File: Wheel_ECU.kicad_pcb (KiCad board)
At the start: 2 copper layers, 61 x 61 mm, 57 parts, among them J1 Conn_01x04, J2 Conn_01x04, J3 Conn_01x02, J4 Debug, U1 IFX9201SG, U2 TLE4964, U3 XMC1404_F064, U4 TLE7251

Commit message: Increase motor hole again and remove two mount holes
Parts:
- removed the M** at (140.1, 90.1)
- removed the M** at (123.5, 106.7)
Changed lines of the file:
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@@
     (tracks 440)
     (zones 0)
-    (modules 57)
+    (modules 55)
     (nets 63)
   )
@@
     (mod_text_size 1 1)
     (mod_text_width 0.15)
-    (pad_size 11.55 5)
-    (pad_drill 9.75)
+    (pad_size 10 10)
+    (pad_drill 10)
     (pad_to_mask_clearance 0.2)
     (aux_axis_origin 0 0)
@@
       (effects (font (size 1 1) (thickness 0.15)))
     )
-    (pad "" np_thru_hole circle (at 0 0) (size 10 10) (drill 10) (layers *.Cu *.Mask)
-      (solder_mask_margin 0.5) (clearance 0.75))
+    (pad "" np_thru_hole circle (at 0 0) (size 10 10) (drill 10) (layers *.Cu *.Mask))
+  )
+  (module WheelECU:Mount_Hole_M3x6.5 (layer F.Cu)
+    (at 123.5 90.1 135)
+    (fp_text reference M** (at -1.2 3.2 135) (layer F.SilkS) hide
+      (effects (font (size 1 1) (thickness 0.15)))
+    )
+    (fp_text value Motor_Mount_Hole (at 0 -3.5 135) (layer F.Fab) hide
+      (effects (font (size 1 1) (thickness 0.15)))
+    )
+    (pad "" np_thru_hole oval (at 0 0 135) (size 9.75 3.2) (drill oval 9.75 3.2) (layers *.Cu *.Mask)
+      (solder_mask_margin 1.2) (clearance 1.4))
   )
   (module Diodes_SMD:D_MELF (layer F.Cu)
@@
   )
   (module WheelECU:Mount_Hole_M3x6.5 (layer F.Cu)
-    (at 140.1 90.1 45)
-    (fp_text reference M** (at -1.2 3.2 45) (layer F.SilkS) hide
-      (effects (font (size 1 1) (thickness 0.15)))
-    )
-    (fp_text value Motor_Mount_Hole (at 0 -3.5 45) (layer F.Fab) hide
-      (effects (font (size 1 1) (thickness 0.15)))
-    )
-    (pad "" np_thru_hole oval (at 0 0 45) (size 9.75 3.2) (drill oval 9.75 3.2) (layers *.Cu *.Mask)
-      (solder_mask_margin 1.2) (clearance 1.4))
-  )
-  (module WheelECU:Mount_Hole_M3x6.5 (layer F.Cu)
-    (at 123.5 106.7 45)
-    (fp_text reference M** (at -1.2 3.2 45) (layer F.SilkS) hide
-      (effects (font (size 1 1) (thickness 0.15)))
-    )
-    (fp_text value Motor_Mount_Hole (at 0 -3.5 45) (layer F.Fab) hide
-      (effects (font (size 1 1) (thickness 0.15)))
-    )
-    (pad "" np_thru_hole oval (at 0 0 45) (size 9.75 3.2) (drill oval 9.75 3.2) (layers *.Cu *.Mask)
-      (solder_mask_margin 1.2) (clearance 1.4))
-  )
-  (module WheelECU:Mount_Hole_M3x6.5 (layer F.Cu)
-    (at 123.5 90.1 135)
-    (fp_text reference M** (at -1.2 3.2 135) (layer F.SilkS) hide
-      (effects (font (size 1 1) (thickness 0.15)))
-    )
-    (fp_text value Motor_Mount_Hole (at 0 -3.5 135) (layer F.Fab) hide
-      (effects (font (size 1 1) (thickness 0.15)))
-    )
-    (pad "" np_thru_hole oval (at 0 0 135) (size 9.75 3.2) (drill oval 9.75 3.2) (layers *.Cu *.Mask)
-      (solder_mask_margin 1.2) (clearance 1.4))
-  )
-  (module WheelECU:Mount_Hole_M3x6.5 (layer F.Cu)

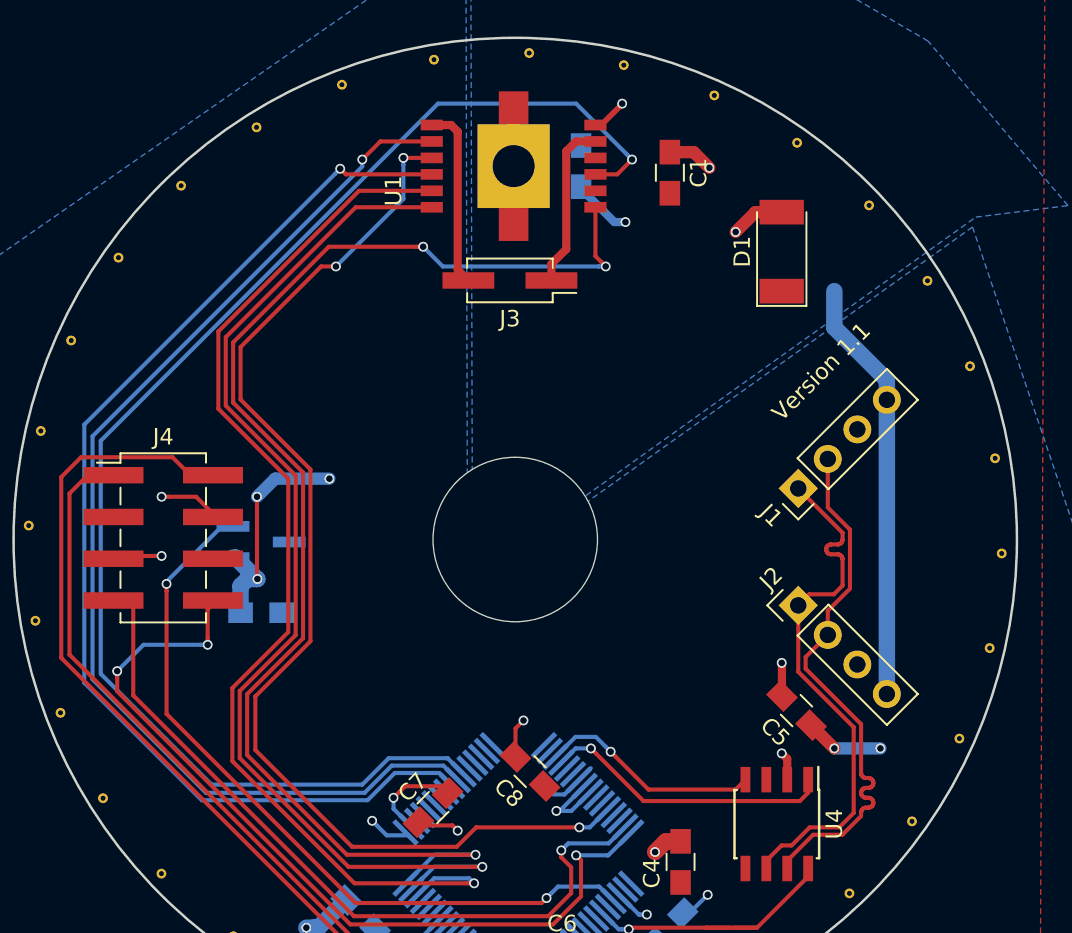
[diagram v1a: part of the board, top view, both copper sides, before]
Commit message: Supply the motor directly from the battery
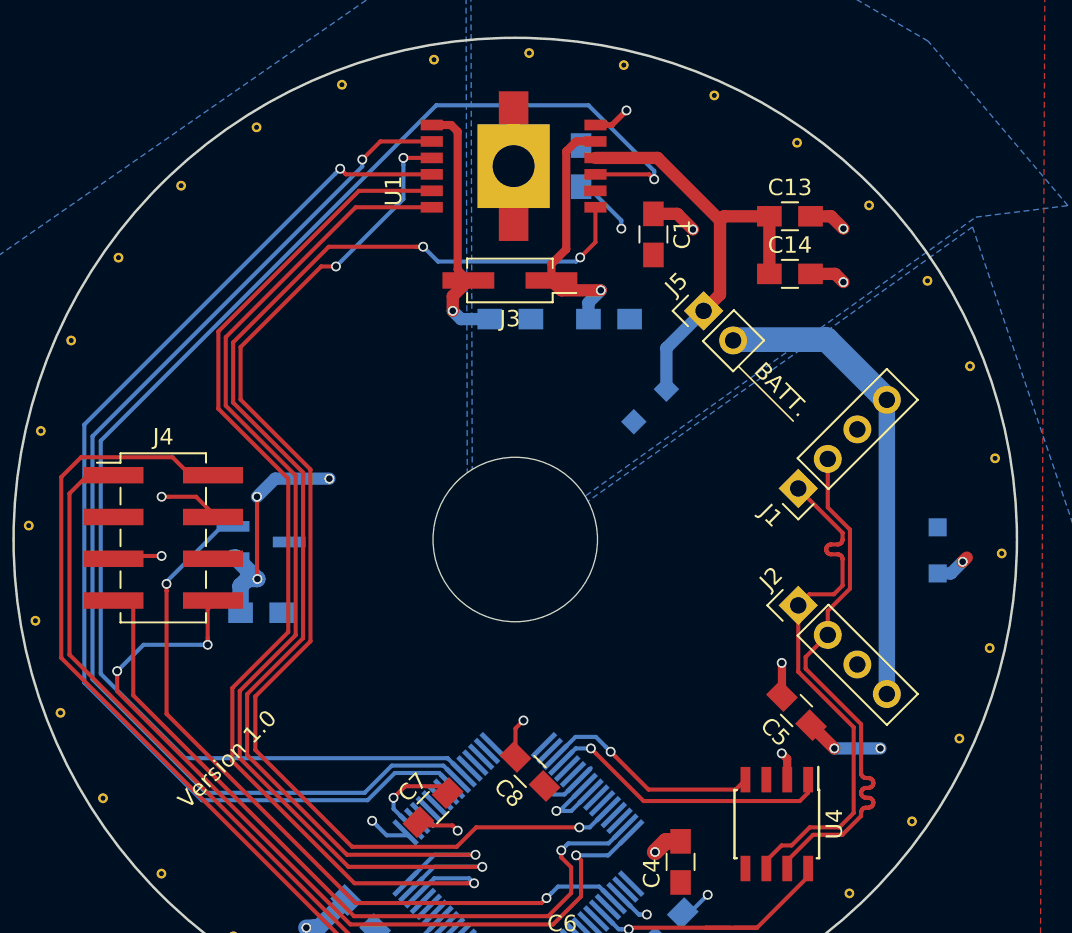
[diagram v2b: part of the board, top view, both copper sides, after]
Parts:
- added C11: 30nF, WheelECU:C_0805_HandSoldering, B.Cu at (131.5, 85.0)
- added C12: 30nF, WheelECU:C_0805_HandSoldering, B.Cu at (137.5, 85.0)
- added C13: 100uF, WheelECU:C_0805_HandSoldering, F.Cu at (148.5, 78.8)
- added C14: 100nF, WheelECU:C_0805_HandSoldering, F.Cu at (148.5, 82.2)
- added D2: SMF36A, Diode_SMD:D_SOD-123F, B.Cu at (140.0, 90.2)
- added J5: Conn_01x02, Connector_PinHeader_2.54mm:PinHeader_1x02_P2.54mm_Vertical, F.Cu at (143.2, 84.5)
- D1: footprint Diodes_SMD:D_MELF -> Diode_SMD:D_SOD-123F; moved to B.Cu
- moved D1 20.5 mm to (157.5, 99.1)
- moved C1 3.88 mm to (140.2, 79.8)
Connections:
- U1 pad 4: +5V -> +BATT
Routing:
- net +BATT: track 0.00 -> 27.4 mm
- net MOTOR_OUT1: track 10.2 -> 15.6 mm, vias 0 -> 1
- net MOTOR_OUT2: track 11.1 -> 15.8 mm, vias 0 -> 1
- net GND: track 77.9 -> 82.2 mm, vias 12 -> 13
- net +5V: track 44.8 -> 47.1 mm, vias 12 -> 13
- net MOTOR_DIRECTION: track 78.8 -> 76.8 mm
- net MISO: track 85.0 -> 86.8 mm
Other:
- board text added: "BATT."
- board text added: "Version 1.0"
- board text removed: "Version 1.1"

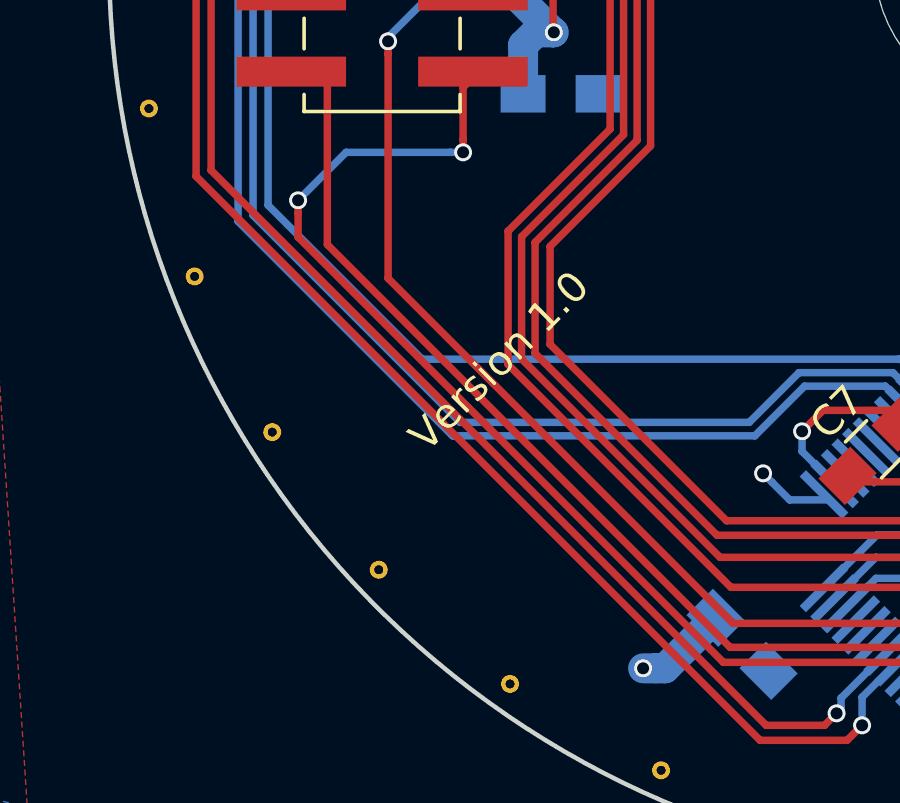
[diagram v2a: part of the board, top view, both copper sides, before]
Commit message: Update the name and version text on the PCB
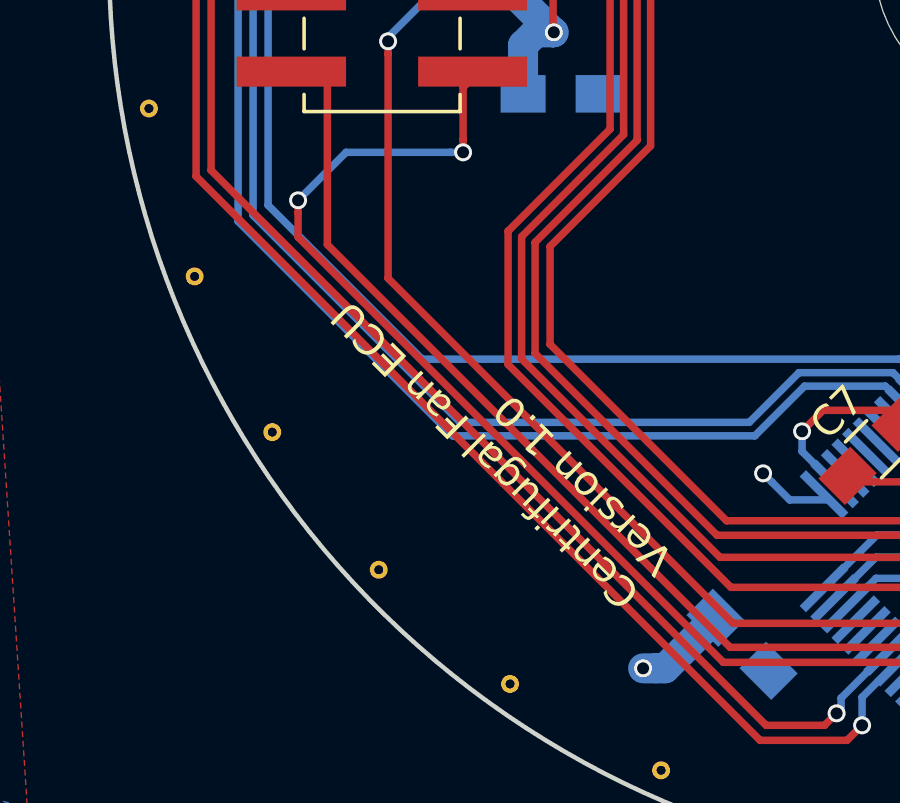
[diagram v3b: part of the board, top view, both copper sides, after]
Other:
- board text added: "Centrifugal Fan ECU Version 1.0"
- board text removed: "Version 1.0"
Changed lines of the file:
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@@
     (arrow2b (pts (xy 101.3 59.5) (xy 102.426504 58.913579)))
   )
-  (gr_text "Version 1.0" (at 114.3 111.76 45) (layer F.SilkS)
-    (effects (font (size 1 1) (thickness 0.15)))
+  (gr_text "Centrifugal Fan ECU\nVersion 1.0" (at 119.3 119.2 135) (layer F.SilkS)
+    (effects (font (size 1 1) (thickness 0.15)) (justify left))
   )
   (segment (start 154.392103 107.792103) (end 154.392103 89.907897) (width 1) (layer B.Cu) (net 1))

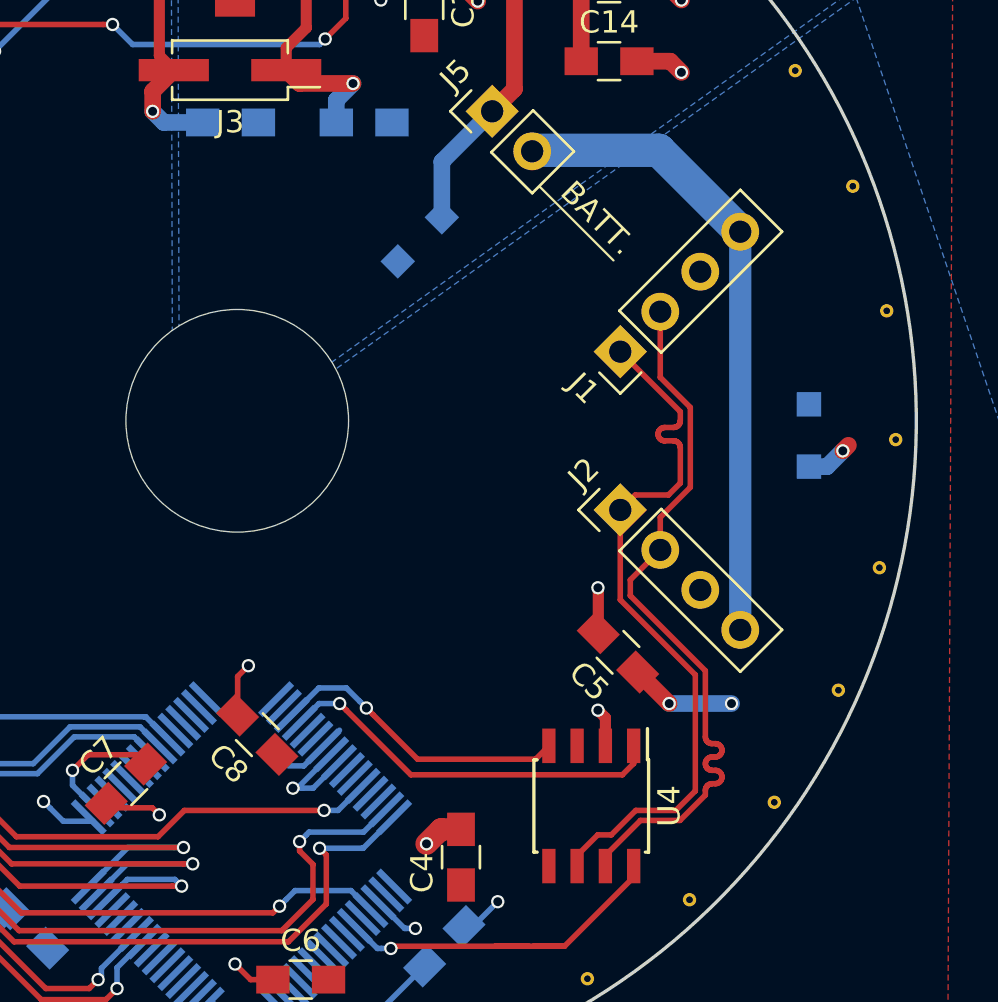
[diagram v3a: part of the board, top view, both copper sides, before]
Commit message: Make room for a bigger motor on the PCB
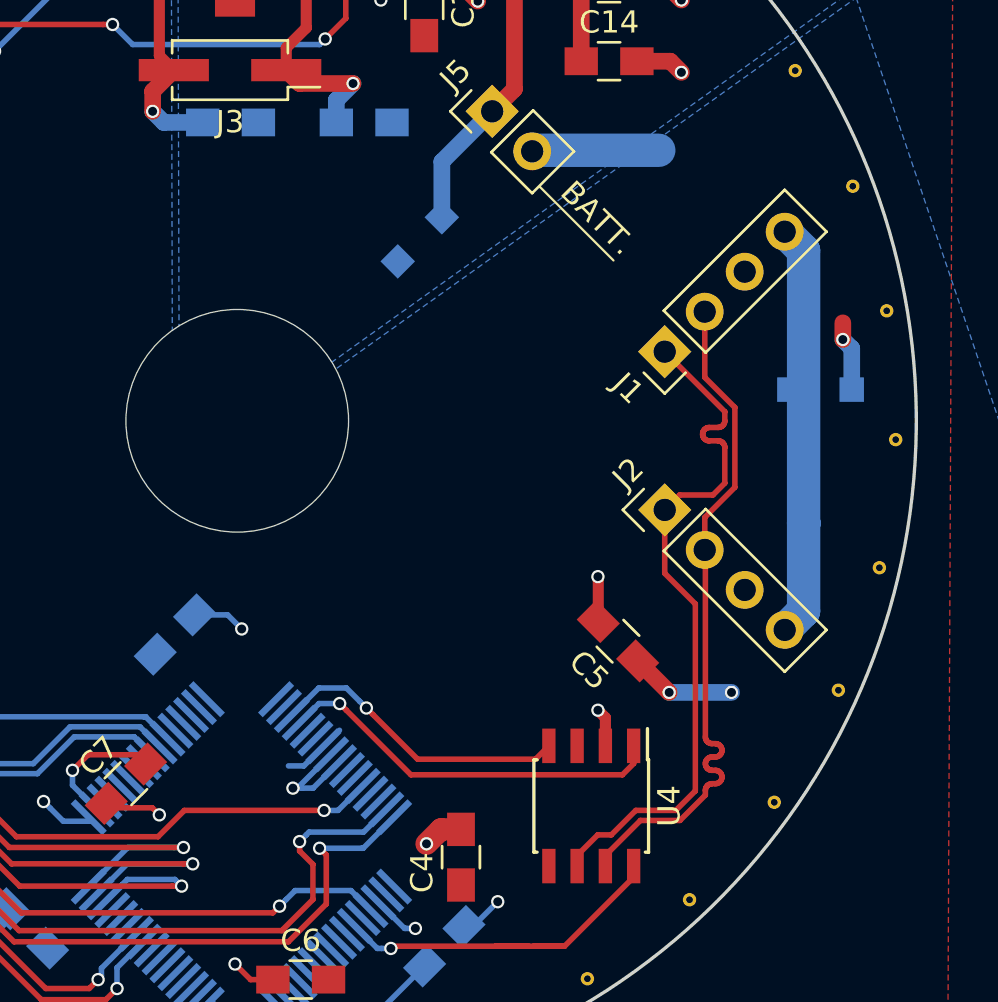
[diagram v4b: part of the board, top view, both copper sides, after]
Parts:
- C8: moved to B.Cu
- moved C8 5.83 mm to (129.0, 108.0), turned to 45 degrees
- moved D1 2.12 mm to (158.0, 97.0), turned to 180 degrees
- moved J1 2.00 mm to (151.0, 95.3)
- moved J2 2.00 mm to (151.0, 102.4)
- moved C5 0.50 mm to (148.9, 108.3)
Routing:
- net GND: track 82.2 -> 75.3 mm, vias 13 -> 12
- net +5V: track 47.1 -> 50.5 mm, vias 13 -> 14
- net CAN+: track 32.8 -> 30.9 mm
- net CAN-: track 32.7 -> 31.9 mm

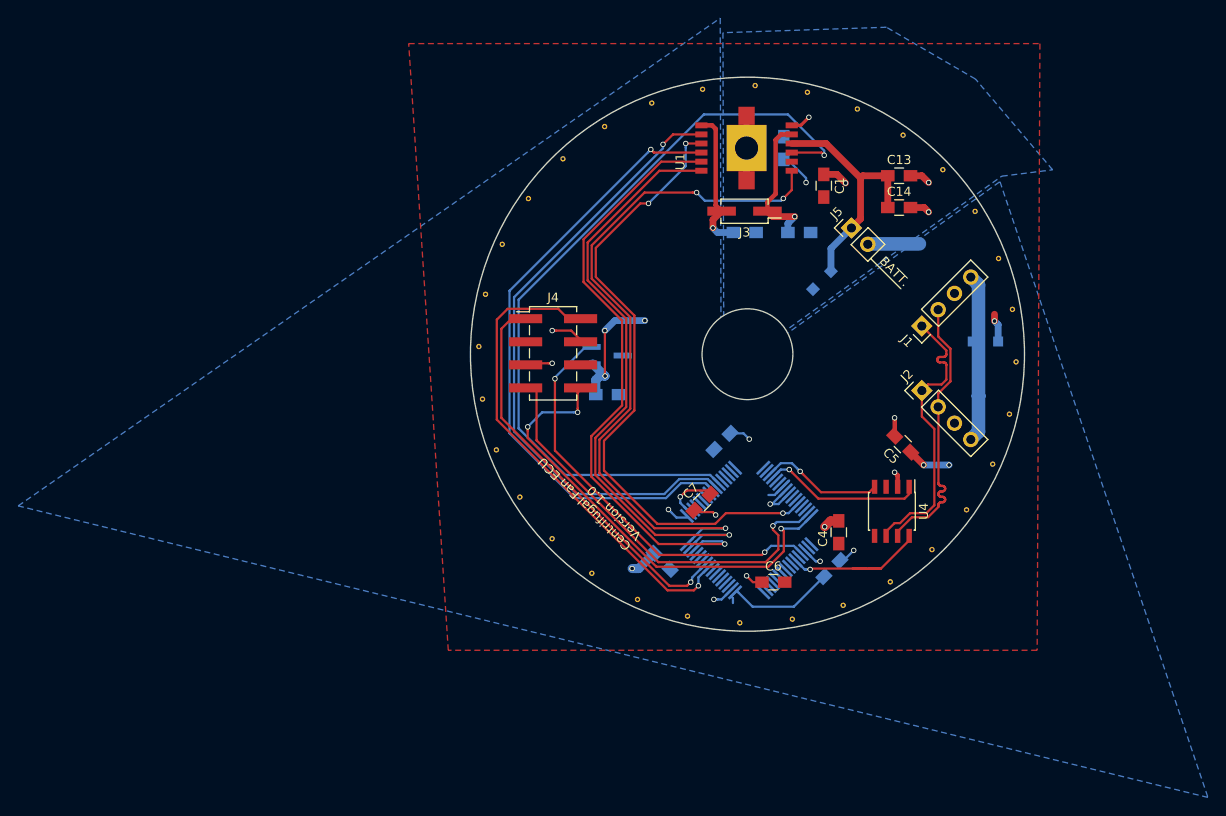
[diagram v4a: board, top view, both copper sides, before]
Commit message: Improve the placement of the motor driver and connector
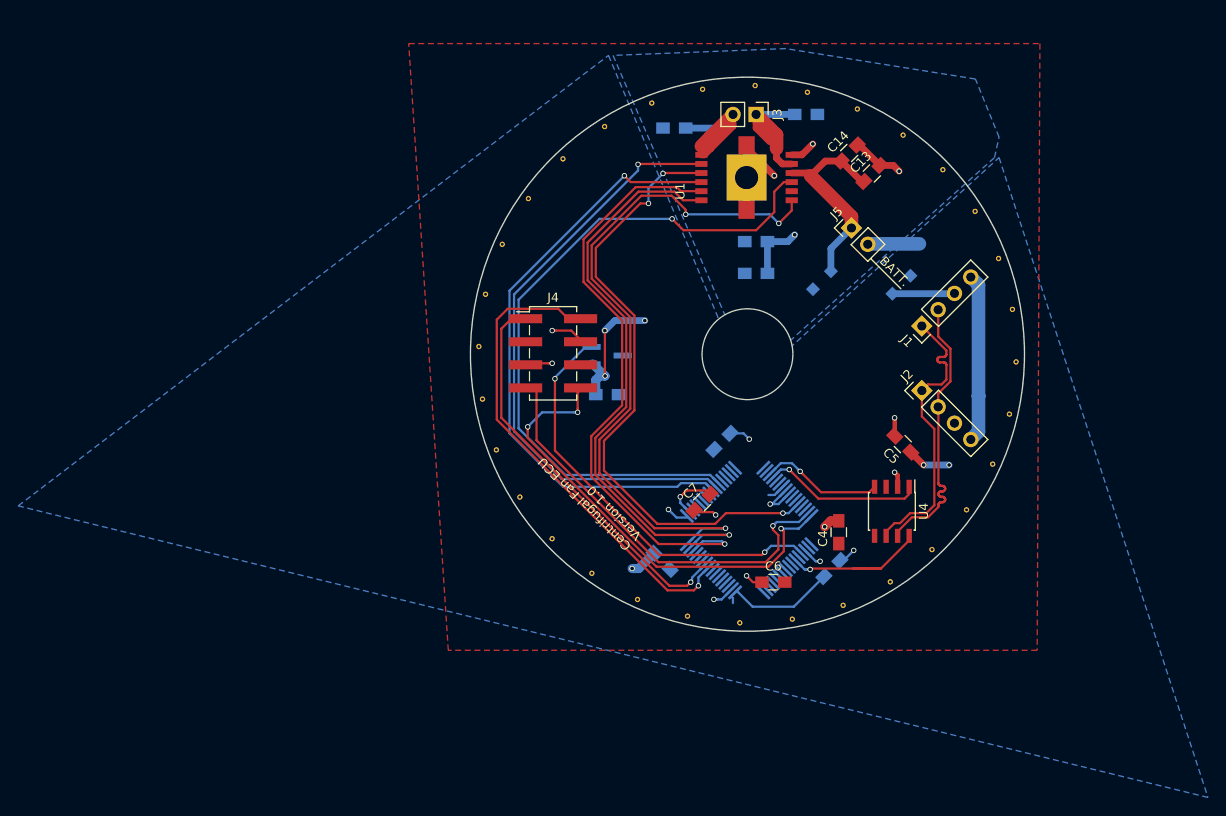
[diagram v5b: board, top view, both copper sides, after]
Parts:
- C1: moved to B.Cu
- J3: footprint Pin_Headers:Pin_Header_Straight_2x01_Pitch2.54mm_SMD -> Connector_PinHeader_2.54mm:PinHeader_1x02_P2.54mm_Vertical
- moved C10 14.1 mm to (132.8, 89.5), turned to 0 degrees
- moved C11 13.9 mm to (123.8, 73.5), turned to 180 degrees
- moved C12 13.0 mm to (138.2, 72.0)
- moved D1 11.2 mm to (148.8, 90.8), turned to 45 degrees
- moved J3 10.7 mm to (132.8, 72.0), turned to 270 degrees
- moved C1 9.66 mm to (132.8, 86.0), turned to 0 degrees
- moved C14 8.14 mm to (143.0, 76.2), turned to 45 degrees
- moved U1 3.25 mm to (131.7, 79.0)
- moved C13 3.01 mm to (145.5, 78.5), turned to 45 degrees
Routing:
- net MISO: track 86.8 -> 76.6 mm
- net +5V: track 50.5 -> 57.1 mm, vias 14 -> 13
- net +BATT: track 27.4 -> 23.0 mm
- net GND: track 75.3 -> 79.0 mm, vias 12 -> 11
- net MOTOR_OUT2: track 15.8 -> 19.1 mm, vias 1 -> 0
- net MOSI: track 69.2 -> 66.8 mm
- net SCLK: track 69.7 -> 67.6 mm
- net MOTOR_DRIVER_SS: track 70.3 -> 68.5 mm
- net MOTOR_DISABLE: track 67.6 -> 66.6 mm
- net MOTOR_PWM: track 66.7 -> 66.1 mm
- net MOTOR_OUT1: vias 1 -> 0
